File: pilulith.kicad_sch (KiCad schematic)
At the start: 82 parts, among them J101 Conn_01x03_Pin, Q1 SBC847, SW101 CK_KMS2xxG, SW102 CK_KMS2xxG, U10 LIS2DH, U101 NRF52840-CKAA-F-R, U102 WLA.04, U103 ATECC608B-MAHDA, U104 LF21115TMR, U105 BME280, U106 MP34DT05TR-A, Y101 32MHz, Y102 32.768K

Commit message: Modified to use nRF54L15 and DFN instead of BGA nRF52. Moving parts to match
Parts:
- removed C106, C110, C112: 0.1U, Capacitor_SMD:C_0201_0603Metric, symbol Device:C_Small
- removed C111: 4U7, Capacitor_SMD:C_0603_1608Metric, symbol Device:C_Small
- removed C113, C114, C115, C116: 12P, Capacitor_SMD:C_0201_0603Metric, symbol Device:C_Small
- removed C119, C120: 560P, Capacitor_SMD:C_0201_0603Metric, symbol Device:C_Small
- removed SW101: CK_KMS2xxG, Button_Switch_SMD:SW_SPST_CK_KMS2xxGP, symbol Switch:CK_KMS2xxG
- removed U101: NRF52840-CKAA-F-R, orleon:BGA_0.25mm_94C35P10X10_360X354X51N, symbol NRF52840-CKAA-F-R:NRF52840-CKAA-F-R
- added C1, C2: 560P, Capacitor_SMD:C_0201_0603Metric, symbol Device:C_Small
- added C3, C5, C7: 2U2, Capacitor_SMD:C_0201_0603Metric, symbol Device:C_Small
- added C4: 10N, Capacitor_SMD:C_0201_0603Metric, symbol Device:C_Small
- added C6: 3P9, Capacitor_SMD:C_0201_0603Metric, symbol Device:C_Small
- added C8: 1P2, Capacitor_SMD:C_0201_0603Metric, symbol Device:C_Small
- added J103: Conn_ARM_JTAG_SWD_10, Connector:Tag-Connect_TC2050-IDC-NL_2x05_P1.27mm_Vertical, symbol Connector:Conn_ARM_JTAG_SWD_10
- added L1, L2: FB, Inductor_SMD:L_0201_0603Metric, symbol Device:L_Small
- added L3: 4U7, Inductor_SMD:L_0402_1005Metric, symbol Device:L_Small
- added L4: 2N0, Inductor_SMD:L_0201_0603Metric, symbol Device:L_Small
- added R66: 0, Resistor_SMD:R_0201_0603Metric, symbol Device:R
- added SW1, SW3: KMT221NG, Button_Switch_SMD:SW_Push_1P1T_NO_CK_KMR2, symbol Switch:CK_KMS2xxG
- added TP1, TP2, TP3, TP9: TestPoint, TestPoint:TestPoint_Pad_D1.5mm, symbol Connector:TestPoint
- added U1: NRF54L15-QFAA-R, pilulith:QFN40P600X600X90-49N, symbol NRF54L15-QFAA-R:NRF54L15-QFAA-R
- C108: value 1U -> 10U
- C117: value 12P -> 1P2
- R113, R114: value 1K -> 100K
- R116: footprint Resistor_SMD:R_0603_1608Metric -> Resistor_SMD:R_0402_1005Metric
- SW2: renamed from SW102; value CK_KMS2xxG -> KMT221NG; footprint Button_Switch_SMD:SW_SPST_CK_KMS2xxGP -> Button_Switch_SMD:SW_Push_1P1T_NO_CK_KMR2
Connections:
- net DEC4_6 is gone; now on net VDD_nRF: C108.1
- net ANT_FEED: now also L4.2; no longer L102.2
- net ANT_NRF: now also U1.31 (ANT)
- net BOOT: now also SW2.1, SW1.1, SW3.1, U1.40 (P1.12/ASI(3)/RADIO(3)/AIN5)
- net BUZZER: now also U1.29 (P0.04/GRTCLFCLKOUT)
- net GND: now also C1.2, C2.1, C3.2, C4.2, C5.2, C6.1, C7.2, C8.1, J103.3 (GND), J103.5 (GND), J103.9 (GNDDetect), SW1.2, SW1.SH (B), SW3.2, SW3.SH (B); no longer Y101.2
- net IMU_INT: now also U1.7 (P1.06/ASO(1)/AIN2)
- net LED01: now also U1.37 (P1.09/ASO(2)/RADIO(0))
- net LED02: now also U1.38 (P1.10/ASI(2)/RADIO(1))
- net LED03: now also U1.11 (P2.00)
- net LED04: now also U1.27 (P0.02)
- net LED05: now also U1.28 (P0.03/GRTCPWM)
- net LED06: now also U1.14 (P2.03)
- net LED07: now also U1.13 (P2.02)
- net LED08: now also U1.12 (P2.01)
- net LED10: now also U1.15 (P2.04)
- net LED11: now also U1.16 (P2.05)
- net LED12: now also U1.42 (P1.14/RADIO(5)/AIN7)
- net MAG: now also U1.41 (P1.13/RADIO(4)/AIN6)
- net MIC_CLK: now also U1.6 (P1.05/ASI(0)/RADIO(6)/AIN1)
- net MIC_DATA: now also U1.5 (P1.04/ASO(0)/AIN0)
- net NFC1: now also C1.1, U1.3 (P1.02/NFC1)
- net NFC2: now also C2.2, U1.4 (P1.03/NFC2)
- net RESET_N: now also R66.1, TP2.1, U1.30 (~{RESET}); no longer SW2.1
- net SCL: now also U1.24 (P0.01)
- net SDA: now also U1.23 (P0.00)
- net SWCLK: now also J103.4 (SWCLK/TCK), TP3.1, U1.26 (SWDCLK)
- net SWDIO: now also J103.2 (SWDIO/TMS), TP9.1, U1.25 (SWDIO)
- net VCC: now also J103.1 (VTref), TP1.1; no longer C101.1
- net nRF52_RX: now also J103.8 (NC/TDI/RX), U1.8 (P1.07/ASI(1)/AIN3)
- net nRF52_TX: now also J103.7 (TX), U1.9 (P1.08/CLK16M/EXTREF)
- net at Y102.2: now also U1.1 (P1.00/XL1)
- net at Y101.1: now also U1.35 (XC2)
- net at Y101.3: now also U1.34 (XC1)
- net at Y102.1: now also U1.2 (P1.01/XL2)
- net VDD_nRF: now reaches C107.1
- net VDD_nRF: now also C101.1, U1.10 (VDD), U1.22 (VDD), U1.36 (VDD), U1.47 (VDD), U1.48 (VDD)
- net at R113.1, R114.2: now also U1.39 (P1.11/ASO(3)/RADIO(2)/AIN4)
- net 0.07/TC renamed 2.06/TC
- net 2.06/TC: now also U1.17 (P2.06/TRACECLK)
- net 0.11/T2 renamed 2.09/T2
- net 2.09/T2: now also U1.20 (P2.09/TRACEDATA(2))
- net 0.12/T1 renamed 2.08/T1
- net 2.08/T1: now also U1.19 (P2.08/TRACEDATA(1))
- net 1.00/T0 renamed 2.07/T0
- net 2.07/T0: now also U1.18 (P2.07/TRACEDATA(0)/SWO)
- net 1.09/T3 renamed 2.10/T3
- net 2.10/T3: now also U1.21 (P2.10/TRACEDATA(3))
- new net: J103.10 (~{RESET}), R66.2
- new net: U1.44 (VSS), U1.49 (VSS)
- new net: C8.2, L102.2, L4.1
- new net DCC: L3.2, U1.46 (DCC)
- new net DECA: C3.1, C4.1, L1.1, L2.1, U1.43 (DECA)
- new net DECD: C7.1, L1.2, L3.1, U1.45 (DECD)
- new net DECRF: C5.1, C6.2, L2.2, U1.33 (DECRF)
- no-connect marks 26 -> 3
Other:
- note added: "Add serial / uart to tag connect output (will need to maeke a converter board)"
- moved on the sheet: C101, C103, C105, C107, C108, C117, D101, D102, D103, D104, D105, D106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

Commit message: initial routing complete
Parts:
- removed C103: 10U, Capacitor_SMD:C_0805_2012Metric, symbol Device:C_Small
- removed L2: FB, Inductor_SMD:L_0201_0603Metric, symbol Device:L_Small
- removed TP1, TP16, TP17, TP18, TP19, TP2, TP20, TP3, TP4, TP5, TP6, TP7, TP8, TP9: TestPoint, TestPoint:TestPoint_Pad_D1.5mm, symbol Connector:TestPoint
- added C9: 0.1U, Capacitor_SMD:C_0201_0603Metric, symbol Device:C_Small
- added LED13, LED14, LED15, LED16: RED, LED_SMD:LED_0201_0603Metric, symbol Device:LED_Small
- added R1, R2, R3, R5: R_Small, Resistor_SMD:R_0201_0603Metric, symbol Device:R_Small
- added SW4: KMT221NG, pilulith:SW_EVP-AWED4A, symbol EVP-AWED4A:EVP-AWED4A
- C4: now fitted
- C5: value 2U2 -> 2N2
- C6: value 3P9 -> 0.1U
- U103: now not fitted
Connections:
- net 2.06/TC is gone; now on net LED05: U1.17 (P2.06/TRACECLK)
- net VDD_nRF is gone; now on net VCC: C101.1, C107.1, C108.1, U1.10 (VDD), U1.22 (VDD), U1.36 (VDD), U1.47 (VDD), U1.48 (VDD)
- net 2.07/T0: now also LED16.2 (A)
- net 2.08/T1: now also LED13.2 (A)
- net 2.09/T2: now also LED14.2 (A)
- net 2.10/T3: now also LED15.2 (A)
- net DECA: now also C5.1, U1.33 (DECRF)
- net GND: now also C6.2, U1.32 (VSS_PA), U1.44 (VSS), U1.49 (VSS), C9.2, R1.2, R2.2, R3.2, R5.2, SW4.2; no longer C6.1
- net IMU_INT: now also U1.39 (P1.11/ASO(3)/RADIO(2)/AIN4); no longer U1.7 (P1.06/ASO(1)/AIN2)
- net LED01: now also U1.38 (P1.10/ASI(2)/RADIO(1)); no longer U1.37 (P1.09/ASO(2)/RADIO(0))
- net LED02: now also U1.37 (P1.09/ASO(2)/RADIO(0)); no longer U1.38 (P1.10/ASI(2)/RADIO(1))
- net LED03: now also U1.28 (P0.03/GRTCPWM); no longer U1.11 (P2.00)
- net LED05: no longer U1.28 (P0.03/GRTCPWM)
- net LED06: now also U1.16 (P2.05); no longer U1.14 (P2.03)
- net LED07: now also U1.15 (P2.04); no longer U1.13 (P2.02)
- net LED08: now also U1.14 (P2.03); no longer U1.12 (P2.01)
- net LED09: now also U1.13 (P2.02)
- net LED10: now also U1.12 (P2.01); no longer U1.15 (P2.04)
- net LED11: now also U1.11 (P2.00); no longer U1.16 (P2.05)
- net RESET_N: now also SW4.1
- net VCC: now also C6.1, C9.1
- net BATTERY_MEAS: now reaches R113.1, R114.2
- net BATTERY_MEAS: now also U1.7 (P1.06/ASO(1)/AIN2); no longer U1.39 (P1.11/ASO(3)/RADIO(2)/AIN4)
- removed net DECRF: C5.1, C6.2, U1.33 (DECRF)
- new net: LED16.1 (K), R3.1
- new net: LED15.1 (K), R2.1
- new net: LED14.1 (K), R5.1
- new net: LED13.1 (K), R1.1
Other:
- moved on the sheet: C1, C2, J101, J103, R113, R114, R66

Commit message: putting in a no popped npm2100 for future proofing
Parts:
- removed C102: 100U, Capacitor_SMD:C_1210_3225Metric, symbol Device:C_Small
- removed R116: 0, Resistor_SMD:R_0402_1005Metric, symbol Device:R_Small
- added C10: 22U, Capacitor_SMD:C_0603_1608Metric, symbol Device:C_Small
- added C11, C16: 1N, Capacitor_SMD:C_0201_0603Metric, symbol Device:C_Small
- added C12: 10U, Capacitor_SMD:C_0402_1005Metric, symbol Device:C_Small
- added C13, C14: 2U2, Capacitor_SMD:C_0402_1005Metric, symbol Device:C_Small
- added JP1: npm2100-bridge, Jumper:SolderJumper-3_P1.3mm_Bridged2Bar12_RoundedPad1.0x1.5mm, symbol Jumper:Jumper_3_Bridged12
- added JP2: sensor-bridge, Jumper:SolderJumper-3_P1.3mm_Bridged2Bar12_RoundedPad1.0x1.5mm, symbol Jumper:Jumper_3_Bridged12
- added L2: 2u2, Inductor_SMD:L_0603_1608Metric_Pad1.05x0.95mm_HandSolder, symbol Device:L_Small
- added U2: NPM2100-CAAA-R, pilulith:BGA16N44P4X4_189X191X52N, symbol NPM2100-CAAA-R:NPM2100-CAAA-R
- SW1, SW2, SW3: footprint Button_Switch_SMD:SW_Push_1P1T_NO_CK_KMR2 -> pilulith:KMT221NG
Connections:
- net CR2032_V+: now also C11.1, C12.1, JP1.1 (A), L2.1, U2.C4 (VBAT)
- net GND: now also C10.2, C13.2, C14.2, C16.2, U2.B1 (AVSS1), U2.B2 (AVSS2)
- net SCL: now also U2.D2 (SCL)
- net SDA: now also U2.D3 (SDA)
- net VCC: now also JP1.2 (C), JP2.1 (A); no longer C104.1, C105.1, C118.1, C29.1, D3.1 (K), LS1.1, R115.2, R117.1, R118.1, U10.10 (VDD_IO), U10.9 (VDD), U103.8 (VCC), U104.1 (VCC), U105.6 (VDDIO), U105.8 (VDD), U106.1 (VDD)
- new net: C11.2, C12.2, U2.A4 (PVSS)
- new net SW: L2.2, U2.B4 (SW)
- new net VINT-NPM2100: C10.1, C16.1, U2.A3 (VINT)
- new net VOUT-NPM2100: C14.1, JP1.3 (B), U2.A2 (VOUT)
- new net VOUTLDO-NPM2100: C13.1, JP2.3 (B), U2.A1 (LSOUT/VOUTLDO)
- new net VSENSOR: C104.1, C105.1, C118.1, C29.1, D3.1 (K), LS1.1, R115.2, R117.1, R118.1, U10.10 (VDD_IO), U10.9 (VDD), U103.8 (VCC), U104.1 (VCC), U105.6 (VDDIO), U105.8 (VDD), U106.1 (VDD)
- no-connect marks 3 -> 4

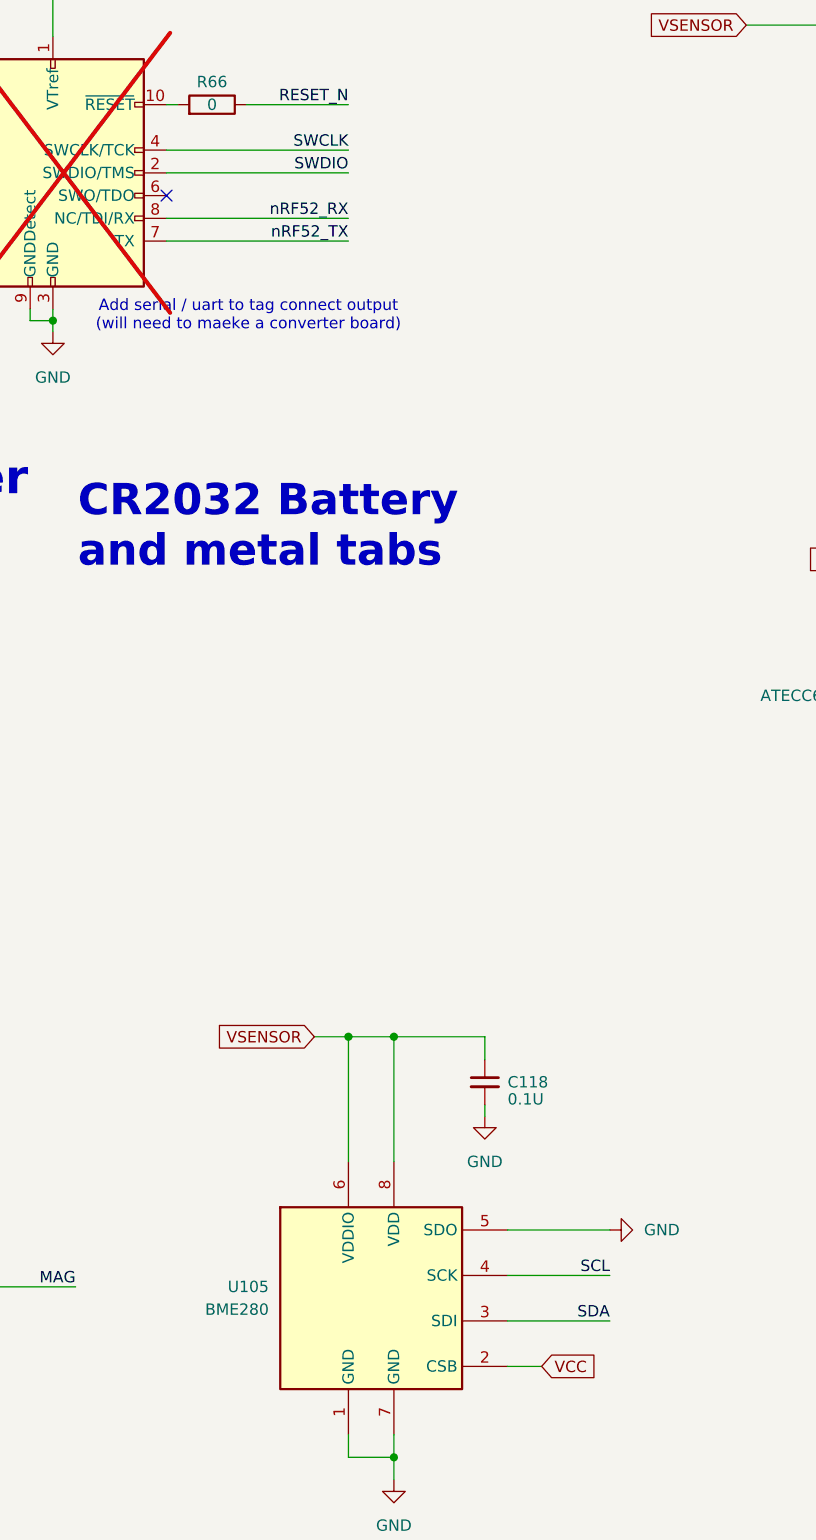
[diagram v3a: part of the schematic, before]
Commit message: rev b first pass done with no violatio ns
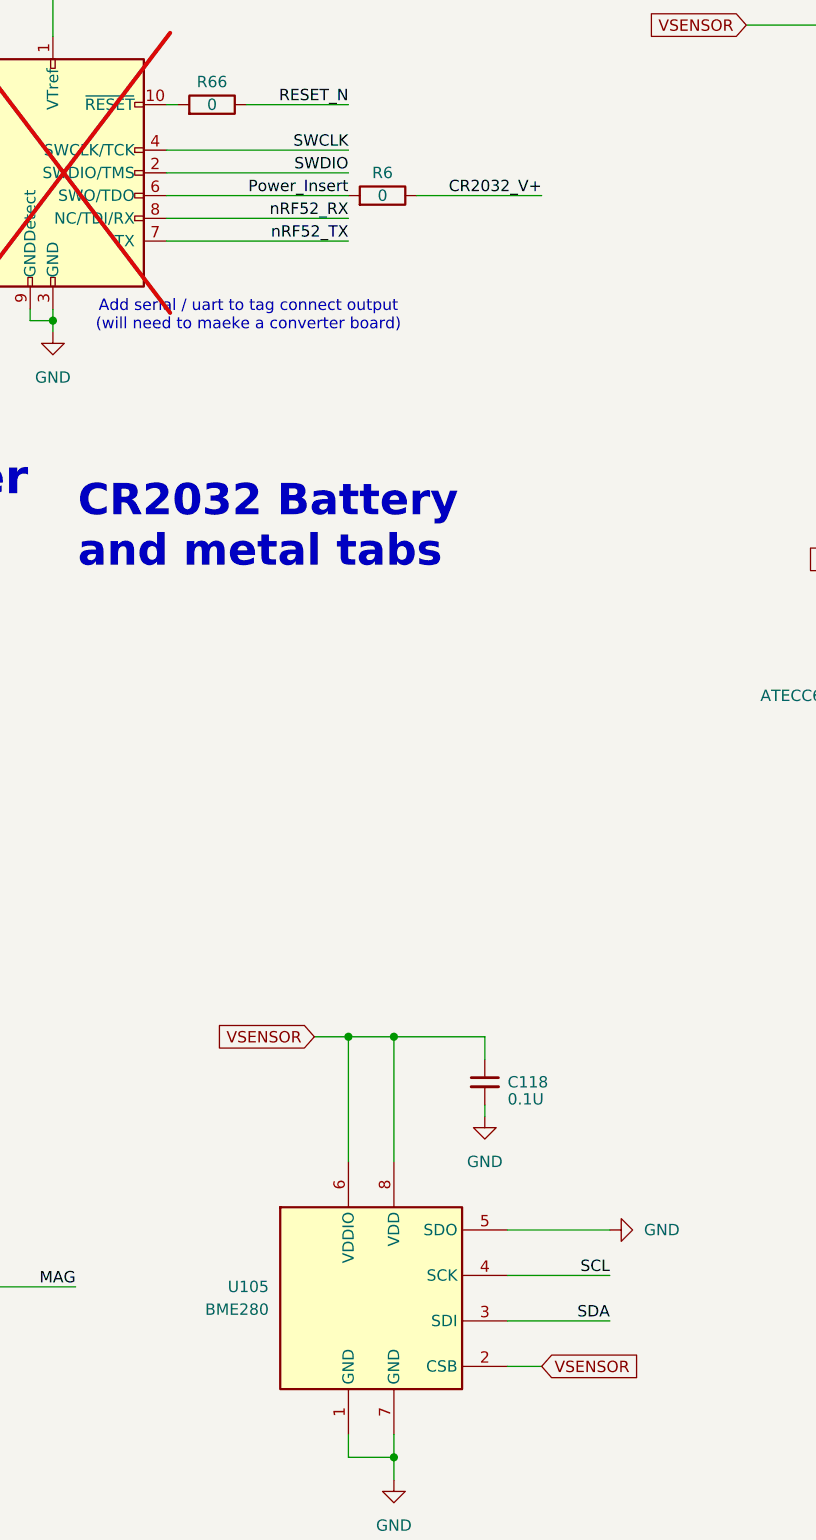
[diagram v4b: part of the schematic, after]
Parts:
- added R6: 0, Resistor_SMD:R_0201_0603Metric, symbol Device:R
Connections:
- net CR2032_V+: now also R6.1
- net VCC: no longer U105.2 (CSB)
- net VSENSOR: now also U105.2 (CSB)
- net Power_Insert: now reaches J103.6 (SWO/TDO)
- net Power_Insert: now also R6.2
- no-connect marks 4 -> 3
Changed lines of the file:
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@@
 	)
 	(no_connect
-		(at 66.04 50.8)
-	)
-	(no_connect
 		(at 370.84 69.85)
 	)
@@
 	(wire
 		(pts
+			(xy 93.98 50.8) (xy 107.95 50.8)
+		)
+		(stroke
+			(width 0)
+			(type default)
+		)
+	)
+	(wire
+		(pts
 			(xy 266.7 64.77) (xy 266.7 82.55)
 		)
@@
 	(wire
 		(pts
+			(xy 66.04 50.8) (xy 86.36 50.8)
+		)
+		(stroke
+			(width 0)
+			(type default)
+		)
+	)
+	(wire
+		(pts
 			(xy 276.86 62.23) (xy 275.59 62.23)
 		)
@@
 		)
 	)
+	(label "Power_Insert"
+		(at 86.36 50.8 180)
+		(effects
+			(font
+				(size 1.27 1.27)
+			)
+			(justify right bottom)
+		)
+	)
 	(label "VOUTLDO-NPM2100"
 		(at 318.77 54.61 0)
@@
 		)
 	)
+	(label "CR2032_V+"
+		(at 107.95 50.8 180)
+		(effects
+			(font
+				(size 1.27 1.27)
+			)
+			(justify right bottom)
+		)
+	)
 	(label "LED09"
 		(at 415.29 214.63 180)
@@
 	(global_label "VCC"
 		(shape input)
-		(at 107.95 181.61 0)
-		(fields_autoplaced yes)
-		(effects
-			(font
-				(size 1.27 1.27)
-			)
-			(justify left)
-		)
-		(property "Intersheetrefs" "${INTERSHEET_REFS}"
-			(at 114.5638 181.61 0)
-			(effects
-				(font
-					(size 1.27 1.27)
-				)
-				(justify left)
-				(hide yes)
-			)
-		)
-	)
-	(global_label "VCC"
-		(shape input)
 		(at 55.88 26.67 0)
 		(fields_autoplaced yes)
@@
 		)
 	)
+	(global_label "VSENSOR"
+		(shape input)
+		(at 107.95 181.61 0)
+		(fields_autoplaced yes)
+		(effects
+			(font
+				(size 1.27 1.27)
+			)
+			(justify left)
+		)
+		(property "Intersheetrefs" "${INTERSHEET_REFS}"
+			(at 119.5228 181.61 0)
+			(effects
+				(font
+					(size 1.27 1.27)
+				)
+				(justify left)
+				(hide yes)
+			)
+		)
+	)
 	(global_label "VCC"
 		(shape input)
@@
 					(unit 1)
 				)
+			)
+		)
+	)
+	(symbol
+		(lib_id "Device:R")
+		(at 90.17 50.8 270)
+		(mirror x)
+		(unit 1)
+		(exclude_from_sim no)
+		(in_bom yes)
+		(on_board yes)
+		(dnp no)
+		(property "Reference" "R6"
+			(at 90.17 48.26 90)
+			(effects
+				(font
+					(size 1.27 1.27)
+				)
+			)
+		)
+		(property "Value" "0"
+			(at 90.17 50.8 90)
+			(effects
+				(font
+					(size 1.27 1.27)
+				)
+			)
+		)
+		(property "Footprint" "Resistor_SMD:R_0201_0603Metric"
+			(at 90.17 52.578 90)
+			(effects
+				(font
+					(size 1.27 1.27)
+				)
+				(hide yes)
+			)
+		)
+		(property "Datasheet" "~"
+			(at 90.17 50.8 0)
+			(effects
+				(font
+					(size 1.27 1.27)
+				)
+				(hide yes)
+			)
+		)
+		(property "Description" ""
+			(at 90.17 50.8 0)
+			(effects
+				(font
+					(size 1.27 1.27)
+				)
+				(hide yes)
+			)
+		)
+		(property "Link1" "https://www.digikey.com/en/products/detail/stackpole-electronics-inc/RMCF0201ZT0R00/1756897"
+			(at 90.17 50.8 0)
+			(effects
+				(font
+					(size 1.27 1.27)
+				)
+				(hide yes)
+			)
+		)
+		(property "MPN1" "RMCF0201ZT0R00"
+			(at 90.17 50.8 0)
+			(effects
+				(font
+					(size 1.27 1.27)
+				)
+				(hide yes)
+			)
+		)
+		(property "Vendor1" "Stackpole Electronics Inc"
+			(at 90.17 50.8 0)
+			(effects
+				(font
+					(size 1.27 1.27)
+				)
+				(hide yes)
+			)
+		)
+		(property "Extra" ""
+			(at 90.17 50.8 0)
+			(effects
+				(font
+					(size 1.27 1.27)
+				)
+			)
+		)
+		(pin "1"
+		)
+		(pin "2"
+		)
+		(instances
+			(project "pilulith"
+				(path "/fdfe0b94-afa6-44ad-a7e5-312f182a8626"
+					(reference "R6")
+					(unit 1)
+				)
